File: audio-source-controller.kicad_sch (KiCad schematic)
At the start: 10 parts, among them K1 AZ850P2-x, K2 AZ850P2-x, K3 AZ850P2-x, U1 ESP32-WROOM-32

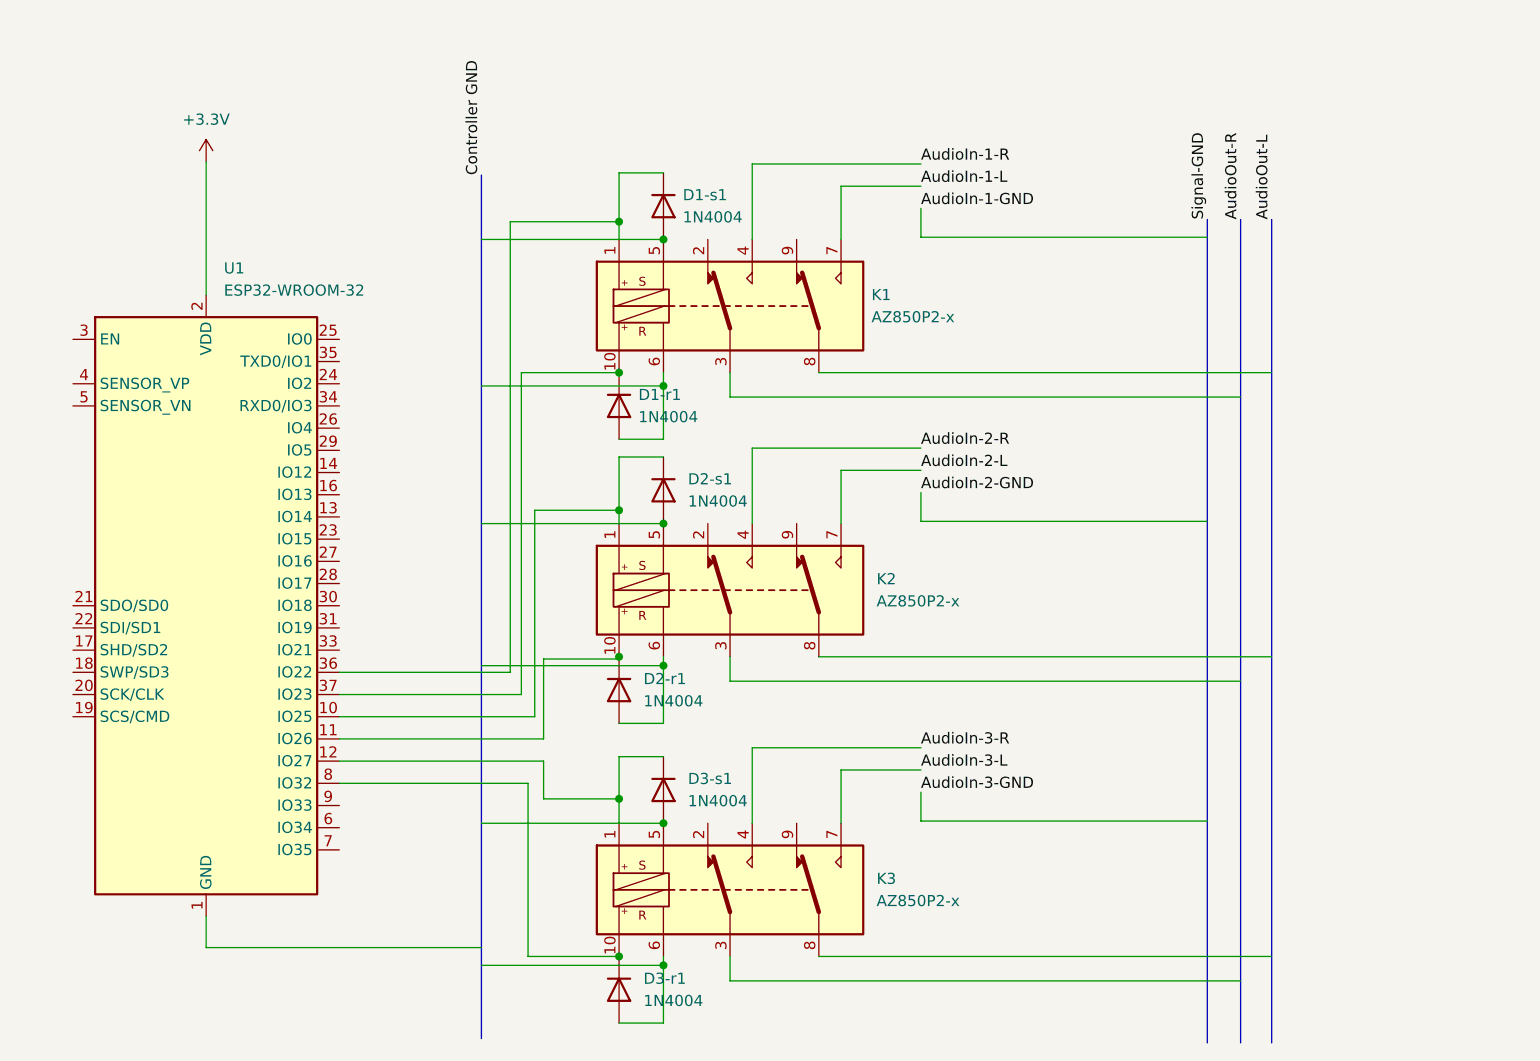
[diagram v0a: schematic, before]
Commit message: Update schematics after ECR
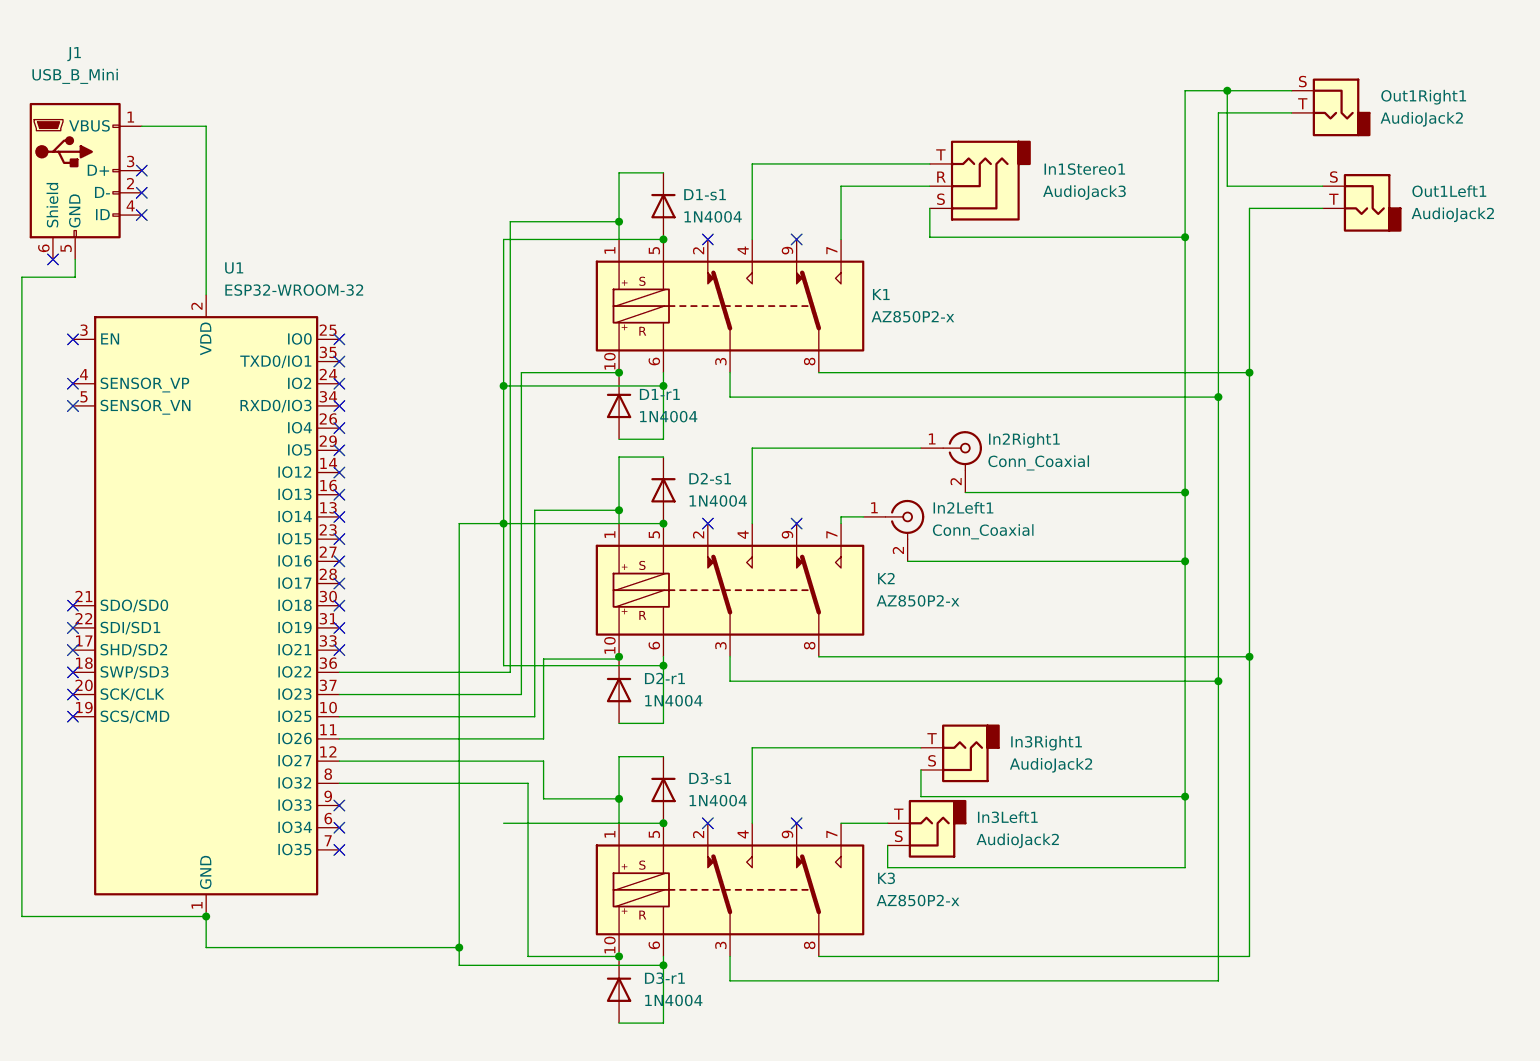
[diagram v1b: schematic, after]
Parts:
- added In1Stereo1: AudioJack3, symbol Connector:AudioJack3
- added In2Left1, In2Right1: Conn_Coaxial, symbol Connector:Conn_Coaxial
- added In3Left1, In3Right1, Out1Left1, Out1Right1: AudioJack2, symbol Connector:AudioJack2
- added J1: USB_B_Mini, symbol Connector:USB_B_Mini
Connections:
- net at D1-r1.2 (A), K1.6: now also D1-s1.2 (A), D2-r1.2 (A), D2-s1.2 (A), D3-r1.2 (A), K1.5, K2.5, K2.6, K3.6, U1.1 (GND), U1.15 (GND), U1.38 (GND), U1.39 (GND), J1.5 (GND)
- net at K2.3: now also K1.3, K3.3, Out1Right1.T
- net at K2.8: now also K1.8, K3.8, Out1Left1.T
- net +3V3: no longer names the net of U1.2 (VDD)
- net +3V3: now also J1.1 (VBUS)
- net AudioIn-1-L: no longer names the net of K1.7
- net AudioIn-1-L: now also In1Stereo1.R
- net AudioIn-1-R: no longer names the net of K1.4
- net AudioIn-1-R: now also In1Stereo1.T
- net AudioIn-2-L: no longer names the net of K2.7
- net AudioIn-2-L: now also In2Left1.1 (In)
- net AudioIn-2-R: no longer names the net of K2.4
- net AudioIn-2-R: now also In2Right1.1 (In)
- net AudioIn-3-L: no longer names the net of K3.7
- net AudioIn-3-L: now also In3Left1.T
- net AudioIn-3-R: no longer names the net of K3.4
- net AudioIn-3-R: now also In3Right1.T
- new net: In1Stereo1.S, In2Left1.2 (Ext), In2Right1.2 (Ext), In3Left1.S, In3Right1.S, Out1Left1.S, Out1Right1.S
- no-connect marks 0 -> 37
